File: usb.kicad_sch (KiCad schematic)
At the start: 118 parts, among them J4 WE_632723300011_alt_symbol, U10 TUSB1046-DCI, U12 AP22615, U13 TPD4E05U06QDQARQ1, U14 TPD4E05U06QDQARQ1, U15 TPD4E05U06QDQARQ1, U16 TPD4E05U06QDQARQ1, U5 FT230XQ-R, U6 TPS65988, U7 W25Q80DVUXIE_TR, U8 NCP730BMT330TBG

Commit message: Schematic Done
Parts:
- removed R205: R_100k_0402, jetson-orin-baseboard-footprints:0402-res, symbol jetson-orin-baseboard:R_100k_0402
- removed U6: TPS65988, jetson-orin-baseboard-footprints:IC_TPS65987DDHRSHR, symbol jetson-orin-baseboard:TPS65988
- added R5: R_100k_0402, jetson-orin-baseboard-footprints:0402-res, symbol jetson-orin-baseboard:R_100k_0402
- added U22: TPS65987, jetson-orin-baseboard-footprints:IC_TPS65987DDHRSHR, symbol jetson-orin-baseboard:TPS65987
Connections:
- net +3V3: now also R5.2, U22.5 (VIN_3V3)
- net +5V: now also U22.25 (PP_CABLE)
- net GND: now also U22.1 (PP_HV2), U22.2 (PP_HV2), U22.20 (GND), U22.45 (GND), U22.46 (GND), U22.47 (GND), U22.51 (GND), U22.59 (GND_EP)
- net PDC_ADCIN1: now also U22.6 (ADCIN1)
- net PDC_ADCIN2: now also U22.10 (ADCIN2)
- net PDC_CTL0: now also U22.17 (GPIO1)
- net PDC_CTL1: now also U22.18 (GPIO2)
- net PDC_FLIP: now also U22.16 (GPIO0)
- net PDC_GPIO14: now also U22.42 (GPIO14/PWM1)
- net PDC_GPIO15: now also U22.43 (GPIO15/PWM2)
- net PDC_HPD2: now also U22.31 (GPIO4)
- net PDC_I2C1_IRQn: now also U22.29 (~{I2C1_IRQ})
- net PDC_I2C1_SCL: now also U22.27 (I2C1_SCL)
- net PDC_I2C1_SDA: now also U22.28 (I2C1_SDA)
- net PDC_I2C2_IRQn: now also U22.34 (~{I2C2_IRQ})
- net PDC_I2C2_SCL: now also U22.32 (I2C2_SCL)
- net PDC_I2C2_SDA: now also U22.33 (I2C2_SDA)
- net PDC_I2C3_SCL: now also U22.21 (I2C3_SCL/GPIO5)
- net PDC_I2C3_SDA: now also U22.22 (I2C3_SDA/GPIO6)
- net PDC_LDO_1V8: now also U22.35 (LDO_1V8)
- net PDC_LDO_3V3: now also U22.9 (LDO_3V3)
- net PDC_MISO: now also U22.36 (SPI_POCI)
- net PDC_MOSI: now also U22.37 (SPI_PICO)
- net PDC_RESET: now also U22.44 (HRESET)
- net PDC_SCLK: now also U22.38 (SPI_CLK)
- net USBC0_5V_PEN: now also U22.49 (GPIO17/PP_EXT2)
- net USBC0_CC1: now also U22.24 (C_CC1)
- net USBC0_CC2: now also U22.26 (C_CC2)
- net USBC0_VBUS: now also U22.13 (VBUS1), U22.14 (VBUS1), U22.3 (VBUS2), U22.4 (VBUS2)
- net ~{PDC_CS}: now also U22.39 (~{SPI_CS})
- net ~{PDC_I2C3_IRQ}: now also U22.23 (~{I2C3_IRQ}/GPIO7)
- net at C76.2, U10.25 (AUX_N): now also R5.1
- net at TP13.1: now also U22.30 (GPIO3/HPD)
- net USBPD2_HV renamed USBPD_HV
- net USBPD_HV: now also U22.11 (PP_HV1), U22.12 (PP_HV1)
- new net: U22.15 (DRAIN1), U22.19 (DRAIN1), U22.52 (DRAIN2), U22.56 (DRAIN2), U22.57 (DRAIN2), U22.58 (DRAIN1), U22.7 (DRAIN2), U22.8 (DRAIN1)
- no-connect marks 9 -> 12
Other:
- moved on the sheet: C10, C11, C12, C140, C141, C143, C144, C148, C149, C27, C29, C31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

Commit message: Schematic V1 and footprints assigned
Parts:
- C31: renamed from C52; footprint (none) -> jetson-orin-baseboard-footprints:0402-cap
- C32: renamed from C76; footprint (none) -> jetson-orin-baseboard-footprints:0402-cap
- C41: renamed from C47; footprint (none) -> jetson-orin-baseboard-footprints:0402-cap
- C42: renamed from C11; footprint (none) -> jetson-orin-baseboard-footprints:0402-cap
- C43: renamed from C9; footprint (none) -> jetson-orin-baseboard-footprints:0402-cap
- C44: renamed from C7; footprint (none) -> jetson-orin-baseboard-footprints:0402-cap
- C46: renamed from C51; footprint (none) -> jetson-orin-baseboard-footprints:0402-cap
- C47: renamed from C12; footprint (none) -> jetson-orin-baseboard-footprints:0402-cap
- C48: renamed from C10; footprint (none) -> jetson-orin-baseboard-footprints:0402-cap
- C49: renamed from C8; footprint (none) -> jetson-orin-baseboard-footprints:0402-cap
- renumbered C49 to C23, C26 to C24, C28 to C25, C30 to C26, C33 to C27, C32 to C28, C36 to C29, C37 to C30, C34 to C33, C54 to C34, C31 to C35, C140 to C36, C141 to C37, C143 to C38, C144 to C39, C55 to C40, C56 to C45, C27 to C50, C29 to C51, C57 to C52, C58 to C53, C60 to C54, C61 to C55, C62 to C56, C63 to C57, C148 to C58, C65 to C60, C149 to C61, D9 to D10, D35 to D4, D4 to D5, D5 to D6, D3 to D7, D2 to D8, D7 to D9, J4 to J3, R41 to R11, R42 to R12, R43 to R13, R44 to R14, R45 to R15, R81 to R16, R130 to R17, R131 to R18, R246 to R19, R262 to R20, R33 to R21, R65 to R22, R244 to R23, R70 to R24, R71 to R25, R68 to R26, R69 to R27, R46 to R28, R5 to R29, R207 to R30, R75 to R31, R56 to R32, R57 to R33, R58 to R34, R59 to R35, R79 to R36, R82 to R37, R83 to R38, R73 to R39, R72 to R40, R85 to R41, R86 to R42, R87 to R43, R88 to R44, R89 to R45, R90 to R46, R91 to R47, R92 to R48, R93 to R49, R94 to R50, R95 to R51, R96 to R52, R97 to R53, R98 to R54, R158 to R55, R84 to R56, R99 to R57, R104 to R58, R109 to R59, R110 to R60, R106 to R61, TP19 to TP10, TP20 to TP11, TP24 to TP12, TP25 to TP13, TP26 to TP14, TP13 to TP15, TP28 to TP16, TP15 to TP17, TP16 to TP18, TP18 to TP9, U15 to U10, U16 to U11, U22 to U2, U7 to U3, U8 to U4, U10 to U6, U13 to U7, U12 to U8, U14 to U9

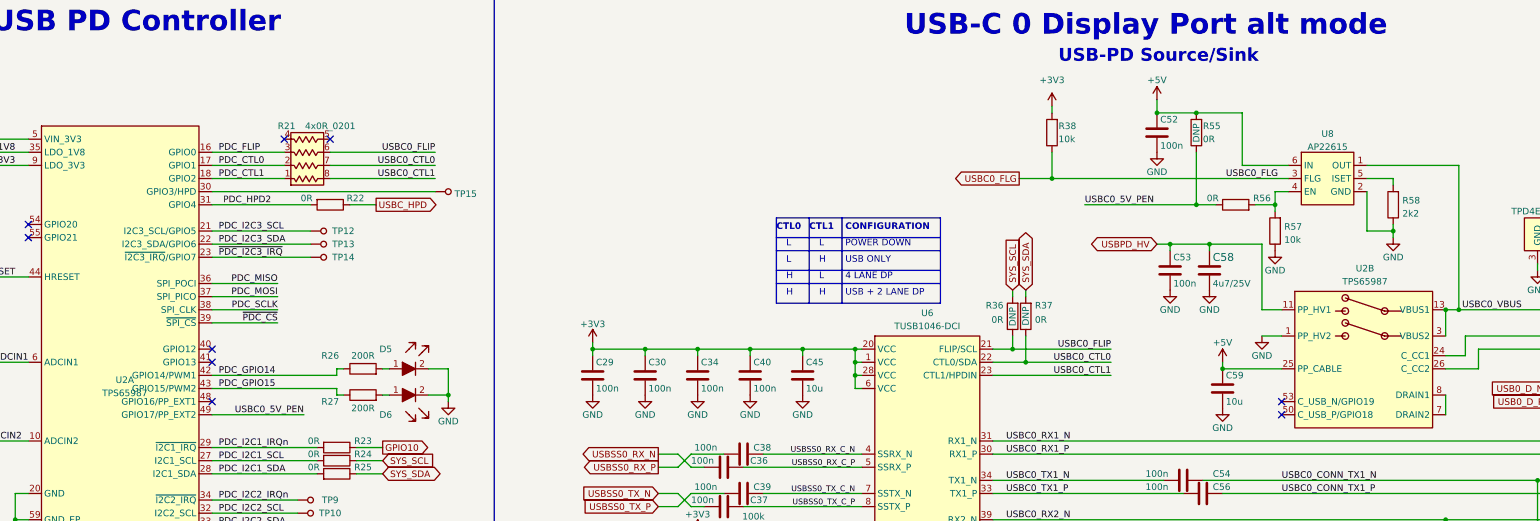
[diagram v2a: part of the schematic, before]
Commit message: New PCB with errors
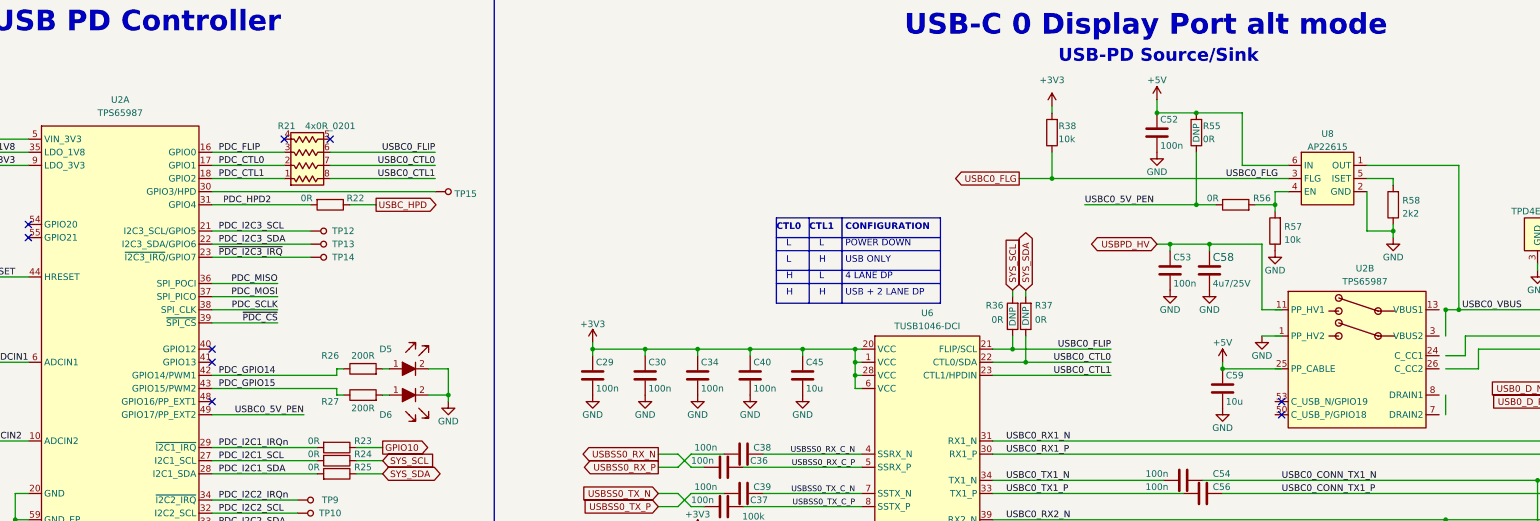
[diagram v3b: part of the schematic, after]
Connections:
- net +5V: no longer U2.25 (PP_CABLE)
- net GND: no longer U2.1 (PP_HV2), U2.2 (PP_HV2)
- net USBC0_CC1: no longer U2.24 (C_CC1)
- net USBC0_CC2: no longer U2.26 (C_CC2)
- net USBC0_VBUS: no longer U2.13 (VBUS1), U2.14 (VBUS1), U2.3 (VBUS2), U2.4 (VBUS2)
- net USBPD_HV: no longer U2.11 (PP_HV1), U2.12 (PP_HV1)
- net at U2.15 (DRAIN1), U2.19 (DRAIN1), U2.58 (DRAIN1)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: no longer U2.52 (DRAIN2), U2.56 (DRAIN2), U2.57 (DRAIN2), U2.7 (DRAIN2)
- new net: U2.52 (DRAIN2), U2.56 (DRAIN2), U2.57 (DRAIN2), U2.7 (DRAIN2)
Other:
- moved on the sheet: U2B
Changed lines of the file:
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@@
   )
   (symbol (lib_name "TPS65987_1") (lib_id "jetson-orin-baseboard:TPS65987") (at 74.93 118.11 0) (unit 1)
-    (in_bom yes) (on_board yes) (dnp no) (fields_autoplaced)
-    (property "Reference" "U2" (at 75.819 87.249 0)
-      (effects (font (size 1.27 1.27)))
-    )
-    (property "Value" "TPS65987" (at 75.819 89.789 0)
+    (in_bom yes) (on_board yes) (dnp no)
+    (property "Reference" "U2" (at 74.93 33.02 0)
+      (effects (font (size 1.27 1.27)))
+    )
+    (property "Value" "TPS65987" (at 74.93 35.56 0)
       (effects (font (size 1.27 1.27)))
     )
@@
     (pin "1")
     (pin "11")
-    (pin "12")
     (pin "13")
-    (pin "14")
     (pin "15")
     (pin "19")
-    (pin "2")
     (pin "24")
     (pin "25")
     (pin "26")
     (pin "3")
-    (pin "4")
     (pin "50")
     (pin "52")
@@
     (pin "1")
     (pin "11")
-    (pin "12")
     (pin "13")
-    (pin "14")
     (pin "15")
     (pin "19")
-    (pin "2")
     (pin "24")
     (pin "25")
     (pin "26")
     (pin "3")
-    (pin "4")
     (pin "50")
     (pin "52")

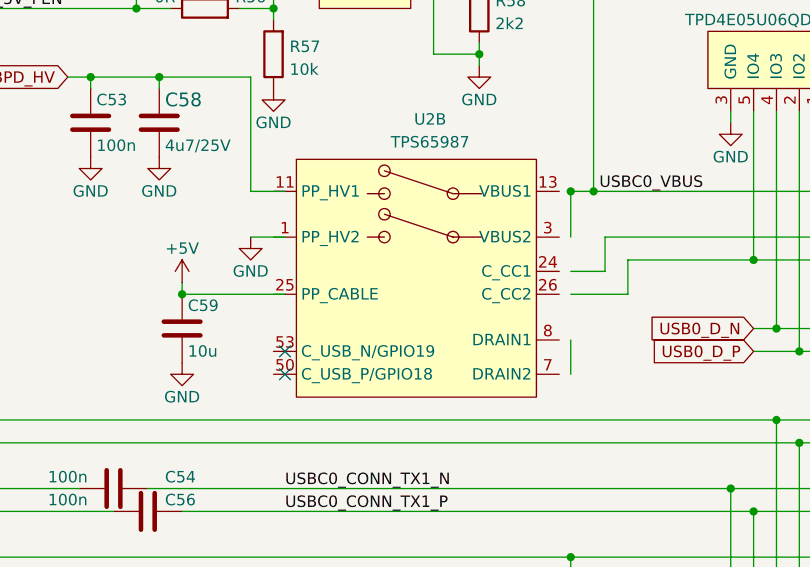
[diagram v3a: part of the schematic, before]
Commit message: Footprints well assigned, XT30 added, Shields grounded
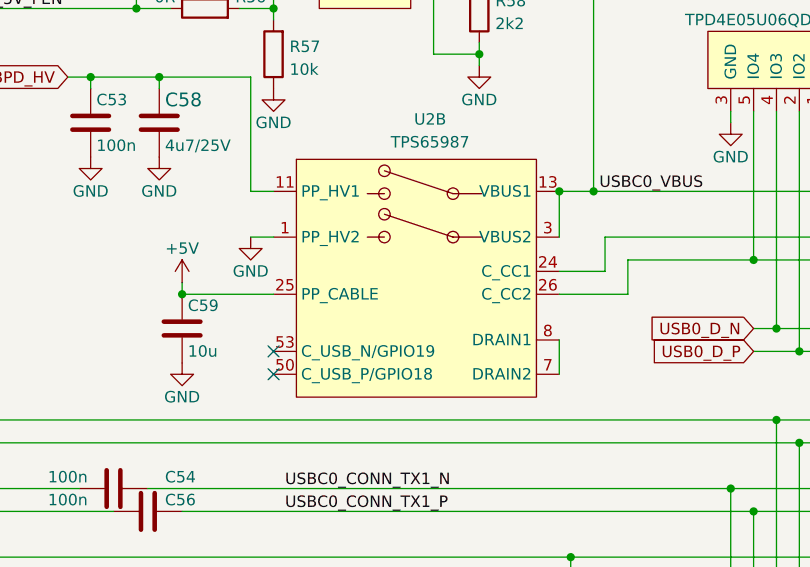
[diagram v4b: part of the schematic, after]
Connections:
- net GND is gone; now on net EP: C23.2, C24.2, C25.2, C26.2, C27.2, C28.2, C29.2, C30.2, C33.2, C34.2, C35.2, C40.2, C45.2, C50.2, C51.2, C52.2, C53.2, C58.2, C59.2, C60.2, C61.2, D10.2, D5.2, D6.2, D9.2, J3.A1 (GND), J3.A12 (GND), J3.B1 (GND), J3.B12 (GND), J3.Shell (SHIELD), R11.1, R13.1, R15.1, R30.2, R42.2, R44.2, R46.2, R48.2, R50.2, R52.2, R54.2, R57.1, R58.1, R59.1, R60.1, U10.3 (GND), U10.8 (GND), U11.3 (GND), U11.8 (GND), U2.20 (GND), U2.45 (GND), U2.46 (GND), U2.47 (GND), U2.51 (GND), U2.59 (GND_EP), U3.4 (VSS), U4.3 (GND), U4.5 (PG), U4.7 (EP), U5.13 (GND), U5.17 (GND), U5.3 (GND), U6.41 (EP_GND), U7.3 (GND), U7.8 (GND), U8.2 (GND), U9.3 (GND), U9.8 (GND)
- net +5V: now also U2.25 (PP_CABLE)
- net USBC0_CC1: now also U2.24 (C_CC1)
- net USBC0_CC2: now also U2.26 (C_CC2)
- net USBC0_VBUS: now also U2.13 (VBUS1), U2.3 (VBUS2)
- net USBPD_HV: now also U2.11 (PP_HV1)
- net EP: now reaches U2.1 (PP_HV2)
- net EP: now also U3.EP
- net at U2.15 (DRAIN1), U2.19 (DRAIN1), U2.58 (DRAIN1)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: now also U2.52 (DRAIN2), U2.56 (DRAIN2), U2.57 (DRAIN2), U2.7 (DRAIN2)
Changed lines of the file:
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@@
   (junction (at 351.79 81.28) (diameter 0) (color 0 0 0 0)
   )
-  (junction (at 331.47 73.66) (diameter 0) (color 0 0 0 0)
-  )
   (junction (at 264.16 147.32) (diameter 0) (color 0 0 0 0)
   )
@@
   (junction (at 71.12 144.78) (diameter 0) (color 0 0 0 0)
   )
-  (junction (at 288.29 85.09) (diameter 0) (color 0 0 0 0)
-  )
   (junction (at 283.21 53.34) (diameter 0) (color 0 0 0 0)
   )
@@
   (junction (at 281.94 152.4) (diameter 0) (color 0 0 0 0)
   )
+  (junction (at 330.2 73.66) (diameter 0) (color 0 0 0 0)
+  )
   (junction (at 265.43 154.94) (diameter 0) (color 0 0 0 0)
   )
@@
   (junction (at 334.01 73.66) (diameter 0) (color 0 0 0 0)
   )
+  (junction (at 288.29 85.09) (diameter 0) (color 0 0 0 0)
+  )
   (junction (at 284.48 149.86) (diameter 0) (color 0 0 0 0)
   )
@@
   (junction (at 307.34 132.08) (diameter 0) (color 0 0 0 0)
   )
-  (no_connect (at 299.72 93.98))
+  (no_connect (at 298.45 93.98))
   (no_connect (at 228.6 242.57))
   (no_connect (at 92.71 83.82))
@@
   (no_connect (at 57.15 59.69))
   (no_connect (at 57.15 57.15))
-  (no_connect (at 299.72 91.44))
+  (no_connect (at 298.45 91.44))
   (no_connect (at 115.57 40.64))
   (no_connect (at 106.68 40.64))
@@
     (stroke (width 0) (type default))
   )
-  (wire (pts (xy 331.47 73.66) (xy 331.47 78.74))
+  (wire (pts (xy 330.2 73.66) (xy 330.2 78.74))
     (stroke (width 0) (type default))
   )
@@
     (stroke (width 0) (type default))
   )
-  (wire (pts (xy 295.91 78.74) (xy 299.72 78.74))
-    (stroke (width 0) (type default))
-  )
   (wire (pts (xy 166.37 247.65) (xy 177.8 247.65))
     (stroke (width 0) (type default))
@@
     (stroke (width 0) (type default))
   )
-  (wire (pts (xy 288.29 85.09) (xy 299.72 85.09))
-    (stroke (width 0) (type default))
-  )
   (wire (pts (xy 284.48 138.43) (xy 284.48 139.7))
     (stroke (width 0) (type default))
@@
     (stroke (width 0) (type default))
   )
+  (wire (pts (xy 295.91 78.74) (xy 298.45 78.74))
+    (stroke (width 0) (type default))
+  )
   (wire (pts (xy 372.11 132.08) (xy 373.38 132.08))
     (stroke (width 0) (type default))
@@
     (stroke (width 0) (type default))
   )
-  (wire (pts (xy 337.82 85.09) (xy 331.47 85.09))
+  (wire (pts (xy 330.2 85.09) (xy 337.82 85.09))
     (stroke (width 0) (type default))
   )
@@
     (stroke (width 0) (type default))
   )
-  (wire (pts (xy 295.91 73.66) (xy 299.72 73.66))
-    (stroke (width 0) (type default))
-  )
   (wire (pts (xy 359.41 78.74) (xy 359.41 64.77))
     (stroke (width 0) (type default))
@@
     (stroke (width 0) (type default))
   )
-  (wire (pts (xy 331.47 73.66) (xy 334.01 73.66))
+  (wire (pts (xy 330.2 73.66) (xy 334.01 73.66))
     (stroke (width 0) (type default))
   )
@@
     (stroke (width 0) (type default))
   )
-  (wire (pts (xy 331.47 90.17) (xy 331.47 93.98))
+  (wire (pts (xy 330.2 90.17) (xy 330.2 93.98))
     (stroke (width 0) (type default))
   )
@@
     (stroke (width 0) (type default))
   )
+  (wire (pts (xy 288.29 85.09) (xy 298.45 85.09))
+    (stroke (width 0) (type default))
+  )
   (wire (pts (xy 196.85 81.28) (xy 196.85 82.55))
     (stroke (width 0) (type default))
@@
     (stroke (width 0) (type default))
   )
-  (wire (pts (xy 331.47 82.55) (xy 335.28 82.55))
+  (wire (pts (xy 330.2 82.55) (xy 335.28 82.55))
     (stroke (width 0) (type default))
   )
@@
     (stroke (width 0) (type default))
   )
+  (wire (pts (xy 295.91 73.66) (xy 298.45 73.66))
+    (stroke (width 0) (type default))
+  )
   (wire (pts (xy 17.78 38.1) (xy 17.78 40.64))
     (stroke (width 0) (type default))
@@
     (pin "7")
     (pin "8")
+    (pin "EP")
     (instances
       (project "jetson-orin-baseboard"
